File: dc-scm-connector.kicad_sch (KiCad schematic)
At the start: 1 part, among them J1 Socket_DC-SCM-2.1_2x84_Rev-1-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

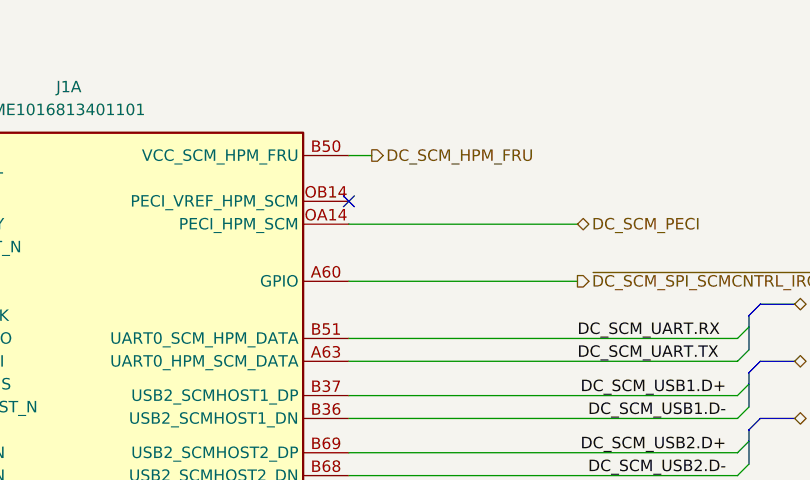
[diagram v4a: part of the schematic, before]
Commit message: [#93514] Change no connect to testpad on PECI line
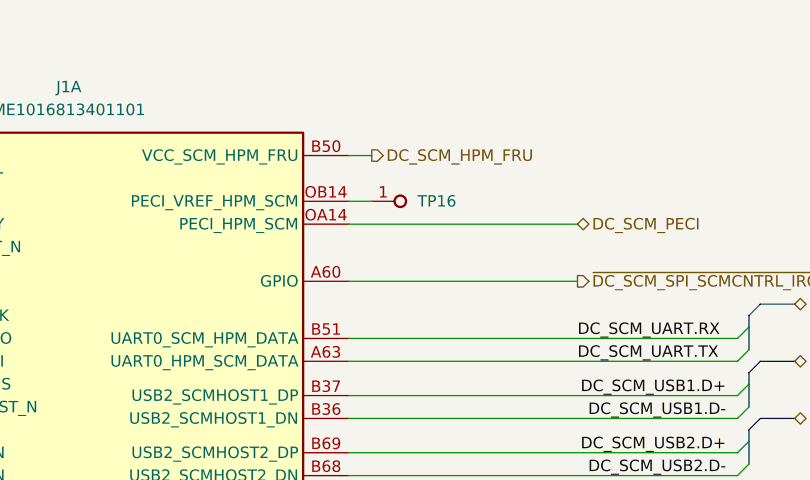
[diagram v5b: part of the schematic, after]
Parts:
- added TP16: TP_0.75mm_SMD, antmicro-footprints:TP_SMD_0.75mm, symbol antmicroTestPoints:TP_0.75mm_SMD
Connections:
- net at J1.OB14 (PECI_VREF_HPM_SCM): now also TP16.1
- no-connect marks 5 -> 4
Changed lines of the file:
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@@
 	)
 	(no_connect
-		(at 147.32 49.53)
-	)
-	(no_connect
 		(at 311.15 172.72)
 	)
@@
 	(wire
 		(pts
+			(xy 149.86 49.53) (xy 147.32 49.53)
+		)
+		(stroke
+			(width 0)
+			(type default)
+		)
+	)
+	(wire
+		(pts
 			(xy 147.32 58.42) (xy 172.72 58.42)
 		)
@@
 			)
 		)
+	)
+	(symbol
+		(lib_id "antmicroTestPoints:TP_0.75mm_SMD")
+		(at 149.86 49.53 0)
+		(unit 1)
+		(exclude_from_sim no)
+		(in_bom no)
+		(on_board yes)
+		(dnp no)
+		(property "Reference" "TP16"
+			(at 154.94 49.53 0)
+			(effects
+				(font
+					(size 1.27 1.27)
+					(thickness 0.15)
+				)
+				(justify left)
+			)
+		)
+		(property "Value" "TP_0.75mm_SMD"
+			(at 160.02 53.34 0)
+			(effects
+				(font
+					(size 1.27 1.27)
+					(thickness 0.15)
+				)
+				(justify left bottom)
+				(hide yes)
+			)
+		)
+		(property "Footprint" "antmicro-footprints:TP_SMD_0.75mm"
+			(at 160.02 55.88 0)
+			(effects
+				(font
+					(size 1.27 1.27)
+					(thickness 0.15)
+				)
+				(justify left bottom)
+				(hide yes)
+			)
+		)
+		(property "Datasheet" ""
+			(at 167.64 62.23 0)
+			(effects
+				(font
+					(size 1.27 1.27)
+					(thickness 0.15)
+				)
+				(justify left bottom)
+				(hide yes)
+			)
+		)
+		(property "Description" "SMT test point"
+			(at 160.655 63.5 0)
+			(effects
+				(font
+					(size 1.27 1.27)
+				)
+				(justify left bottom)
+				(hide yes)
+			)
+		)
+		(property "MPN" ""
+			(at 160.655 60.96 0)
+			(effects
+				(font
+					(size 1.27 1.27)
+					(thickness 0.15)
+				)
+				(justify left bottom)
+				(hide yes)
+			)
+		)
+		(property "Manufacturer" ""
+			(at 160.655 55.88 0)
+			(effects
+				(font
+					(size 1.27 1.27)
+					(thickness 0.15)
+				)
+				(justify left bottom)
+				(hide yes)
+			)
+		)
+		(property "Author" "Antmicro"
+			(at 160.02 58.42 0)
+			(effects
+				(font
+					(size 1.27 1.27)
+					(thickness 0.15)
+				)
+				(justify left bottom)
+				(hide yes)
+			)
+		)
+		(property "License" "Apache-2.0"
+			(at 160.02 60.96 0)
+			(effects
+				(font
+					(size 1.27 1.27)
+					(thickness 0.15)
+				)
+				(justify left bottom)
+				(hide yes)
+			)
+		)
+		(pin "1"
+		)
+		(instances
+			(project "bmc-breakout-board"
+				(path "/5d67ef28-5805-4f87-b722-2926dabf7f6e/bae8cef5-57a9-4ec0-acbe-6dac48c5cdf5"
+					(reference "TP16")
+					(unit 1)
+				)
+			)
+		)

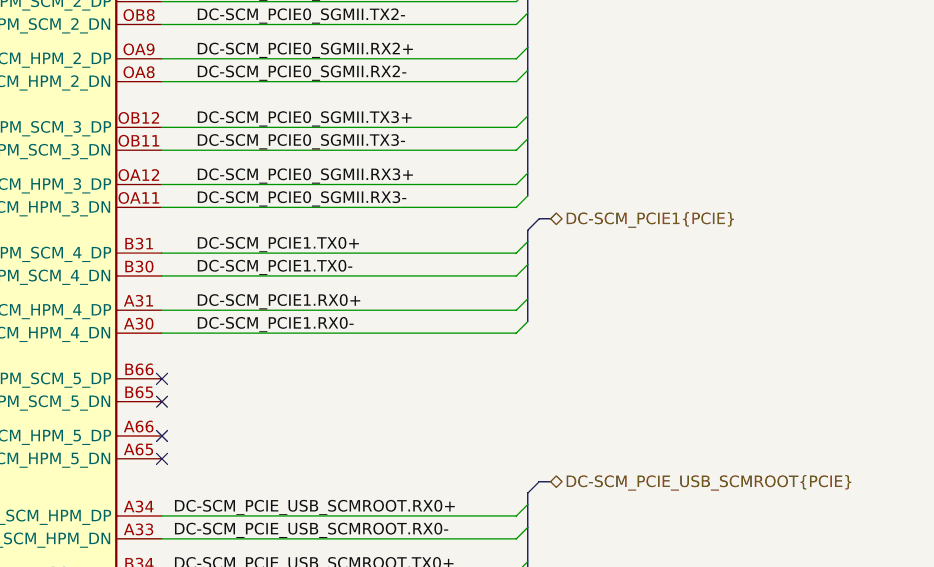
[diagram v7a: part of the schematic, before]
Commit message: [#93514] Add symbolic wire crossing for PCIE1
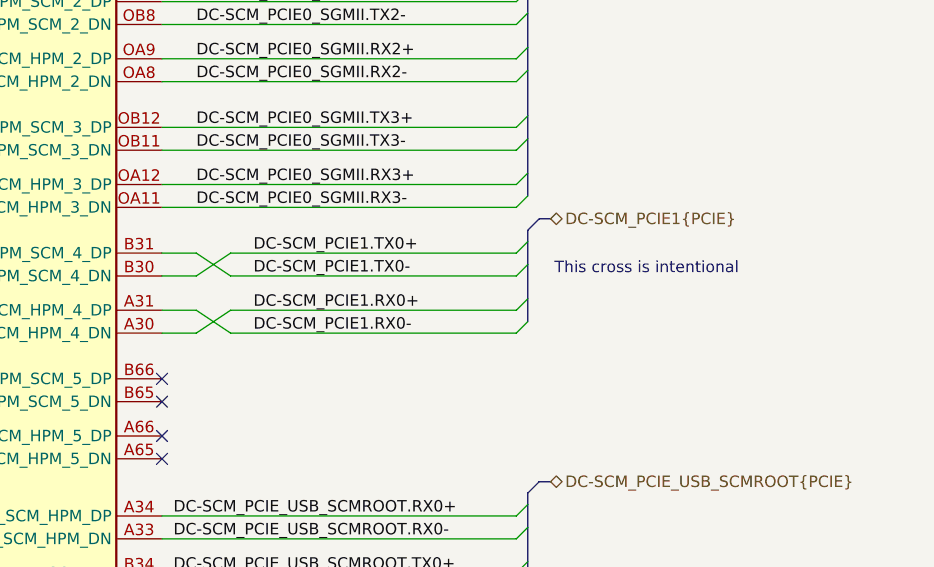
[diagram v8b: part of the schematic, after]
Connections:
- net DC-SCM_PCIE1.RX0+: now also J1.A30 (PCIE_HPMROOT_SCM_HPM_4_DN); no longer J1.A31 (PCIE_HPMROOT_SCM_HPM_4_DP)
- net DC-SCM_PCIE1.RX0-: now also J1.A31 (PCIE_HPMROOT_SCM_HPM_4_DP); no longer J1.A30 (PCIE_HPMROOT_SCM_HPM_4_DN)
- net DC-SCM_PCIE1.TX0+: now also J1.B30 (PCIE_HPMROOT_HPM_SCM_4_DN); no longer J1.B31 (PCIE_HPMROOT_HPM_SCM_4_DP)
- net DC-SCM_PCIE1.TX0-: now also J1.B31 (PCIE_HPMROOT_HPM_SCM_4_DP); no longer J1.B30 (PCIE_HPMROOT_HPM_SCM_4_DN)
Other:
- note added: "This cross is intentional"
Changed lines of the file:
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@@
 		)
 	)
+	(text "This cross is intentional"
+		(exclude_from_sim no)
+		(at 364.998 157.988 0)
+		(effects
+			(font
+				(size 1.27 1.27)
+			)
+		)
+	)
 	(junction
 		(at 81.28 44.45)
@@
 		)
 	)
+	(wire
+		(pts
+			(xy 311.15 156.21) (xy 314.96 156.21)
+		)
+		(stroke
+			(width 0)
+			(type default)
+		)
+	)
 	(bus
 		(pts
@@
 		)
 	)
+	(wire
+		(pts
+			(xy 311.15 162.56) (xy 314.96 162.56)
+		)
+		(stroke
+			(width 0)
+			(type default)
+		)
+	)
 	(bus
 		(pts
@@
 		)
 	)
+	(wire
+		(pts
+			(xy 350.52 156.21) (xy 318.77 156.21)
+		)
+		(stroke
+			(width 0)
+			(type default)
+		)
+	)
 	(bus
 		(pts
@@
 	(wire
 		(pts
+			(xy 318.77 162.56) (xy 314.96 165.1)
+		)
+		(stroke
+			(width 0)
+			(type default)
+		)
+	)
+	(wire
+		(pts
 			(xy 59.69 161.29) (xy 85.09 161.29)
 		)
@@
 	(wire
 		(pts
+			(xy 318.77 156.21) (xy 314.96 158.75)
+		)
+		(stroke
+			(width 0)
+			(type default)
+		)
+	)
+	(wire
+		(pts
 			(xy 311.15 148.59) (xy 350.52 148.59)
 		)
@@
 	(wire
 		(pts
+			(xy 314.96 162.56) (xy 318.77 165.1)
+		)
+		(stroke
+			(width 0)
+			(type default)
+		)
+	)
+	(wire
+		(pts
 			(xy 311.15 91.44) (xy 350.52 91.44)
 		)
@@
 		)
 	)
+	(wire
+		(pts
+			(xy 311.15 165.1) (xy 314.96 165.1)
+		)
+		(stroke
+			(width 0)
+			(type default)
+		)
+	)
 	(bus
 		(pts
@@
 	(wire
 		(pts
+			(xy 311.15 158.75) (xy 314.96 158.75)
+		)
+		(stroke
+			(width 0)
+			(type default)
+		)
+	)
+	(wire
+		(pts
 			(xy 58.42 67.31) (xy 85.09 67.31)
 		)
@@
 		)
 	)
-	(wire
-		(pts
-			(xy 311.15 165.1) (xy 350.52 165.1)
-		)
-		(stroke
-			(width 0)
-			(type default)
-		)
-	)
 	(bus
 		(pts
@@
 	(wire
 		(pts
+			(xy 318.77 158.75) (xy 350.52 158.75)
+		)
+		(stroke
+			(width 0)
+			(type default)
+		)
+	)
+	(wire
+		(pts
 			(xy 66.04 54.61) (xy 85.09 54.61)
 		)
@@
 		)
 	)
-	(wire
-		(pts
-			(xy 311.15 156.21) (xy 350.52 156.21)
-		)
-		(stroke
-			(width 0)
-			(type default)
-		)
-	)
 	(bus
 		(pts
@@
 		)
 	)
-	(wire
-		(pts
-			(xy 311.15 162.56) (xy 350.52 162.56)
-		)
-		(stroke
-			(width 0)
-			(type default)
-		)
-	)
 	(bus
 		(pts
@@
 		)
 	)
+	(wire
+		(pts
+			(xy 350.52 162.56) (xy 318.77 162.56)
+		)
+		(stroke
+			(width 0)
+			(type default)
+		)
+	)
 	(bus
 		(pts
@@
 	(wire
 		(pts
+			(xy 314.96 156.21) (xy 318.77 158.75)
+		)
+		(stroke
+			(width 0)
+			(type default)
+		)
+	)
+	(wire
+		(pts
 			(xy 311.15 114.3) (xy 350.52 114.3)
 		)
@@
 		)
 	)
-	(wire
+	(bus
 		(pts
-			(xy 311.15 158.75) (xy 350.52 158.75)
+			(xy 196.85 67.31) (xy 193.04 67.31)
 		)
 		(stroke
@@
 	(bus
 		(pts
-			(xy 196.85 67.31) (xy 193.04 67.31)
+			(xy 59.69 226.06) (xy 59.69 228.6)
 		)
 		(stroke
@@
 		)
 	)
-	(bus
+	(wire
 		(pts
-			(xy 59.69 226.06) (xy 59.69 228.6)
+			(xy 318.77 165.1) (xy 350.52 165.1)
 		)
 		(stroke
@@
 		)
 	)
+	(label "DC-SCM_PCIE1.TX0+"
+		(at 321.31 156.21 0)
+		(effects
+			(font
+				(size 1.27 1.27)
+			)
+			(justify left bottom)
+		)
+	)
 	(label "DC_SCM_USB1.D-"
 		(at 189.23 73.66 180)
@@
 		)
 	)
-	(label "DC-SCM_PCIE1.RX0-"
-		(at 314.96 165.1 0)
-		(effects
-			(font
-				(size 1.27 1.27)
-			)
-			(justify left bottom)
-		)
-	)
 	(label "DC_SCM_ESPI.SCK"
 		(at 148.59 201.93 0)
@@
 		)
 	)
+	(label "DC-SCM_PCIE1.RX0-"
+		(at 321.31 165.1 0)
+		(effects
+			(font
+				(size 1.27 1.27)
+			)
+			(justify left bottom)
+		)
+	)
 	(label "DC_SCM_UART.TX"
 		(at 172.72 67.31 0)
@@
 		)
 	)
+	(label "DC-SCM_PCIE1.TX0-"
+		(at 321.31 158.75 0)
+		(effects
+			(font
+				(size 1.27 1.27)
+			)
+			(justify left bottom)
+		)
+	)
 	(label "DC_SCM_I2C_I3C12.SDA"
 		(at 152.4 113.03 0)
@@
 		)
 	)
-	(label "DC-SCM_PCIE1.RX0+"
-		(at 314.96 162.56 0)
-		(effects
-			(font
-				(size 1.27 1.27)
-			)
-			(justify left bottom)
-		)
-	)
 	(label "DC-SCM_PCIE0_SGMII.RX1+"
 		(at 314.96 120.65 0)
@@
 		)
 	)
-	(label "DC-SCM_PCIE1.TX0+"
-		(at 314.96 156.21 0)
+	(label "DC-SCM_PCIE1.RX0+"
+		(at 321.31 162.56 0)
 		(effects
 			(font
@@
 		)
 	)
-	(label "DC-SCM_PCIE1.TX0-"
-		(at 314.96 158.75 0)
-		(effects
-			(font
-				(size 1.27 1.27)
-			)
-			(justify left bottom)
-		)
-	)
